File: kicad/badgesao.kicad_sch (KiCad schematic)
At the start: 62 parts, among them J1 DISP_DBG, J2 DEBUG, J3 USB_C_Receptacle_USB2.0_16P, Q1 NPN_BEC, SW1 UP, SW2 DOWN, SW3 LEFT, SW4 RIGHT, SW5 B, SW6 A, SW7 RESET, SW8 BOOTSEL, U1 3V3LDO, U2 32Mb QSPI, U3 LSM6DS3, U4 TPS61022, U6 RP2040, X1 Simple_Addon_v2, Y1 12M

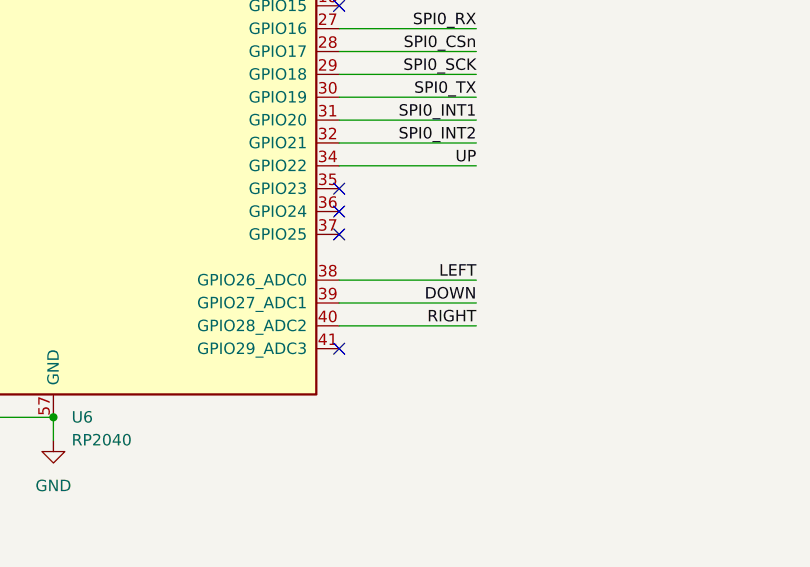
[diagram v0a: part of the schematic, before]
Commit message: connected buzzer and sel nets
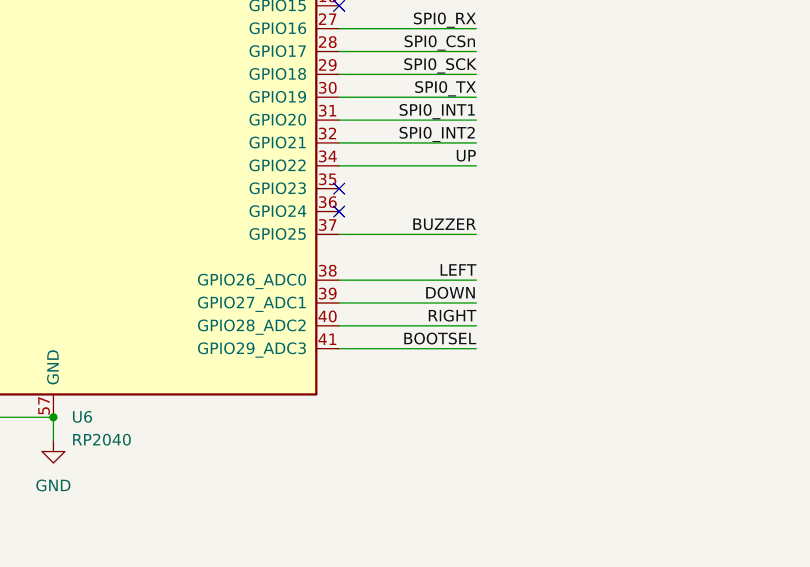
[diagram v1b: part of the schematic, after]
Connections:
- net BOOTSEL: now also U6.41 (GPIO29_ADC3)
- net BUZZER: now also U6.37 (GPIO25)
- no-connect marks 12 -> 10
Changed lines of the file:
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@@
-	)
-	(no_connect
-		(at 151.13 203.2)
 	)
 	(no_connect
@@
 	)
 	(no_connect
-		(at 151.13 215.9)
-	)
-	(no_connect
 		(at 359.41 182.88)
 	)
@@
 	(wire
 		(pts
+			(xy 151.13 215.9) (xy 166.37 215.9)
+		)
+		(stroke
+			(width 0)
+			(type default)
+		)
+	)
+	(wire
+		(pts
 			(xy 276.86 127) (xy 287.02 127)
 		)
@@
 		(pts
 			(xy 151.13 132.08) (xy 162.56 132.08)
+		)
+		(stroke
+			(width 0)
+			(type default)
+		)
+	)
+	(wire
+		(pts
+			(xy 166.37 203.2) (xy 151.13 203.2)
 		)
 		(stroke
@@
 		)
 	)
+	(label "BUZZER"
+		(at 166.37 203.2 180)
+		(fields_autoplaced yes)
+		(effects
+			(font
+				(size 1.27 1.27)
+			)
+			(justify right bottom)
+		)
+	)
 	(label "BLINKENLIGHT"
 		(at 166.37 154.94 180)
@@
 		)
 	)
+	(label "BOOTSEL"
+		(at 166.37 215.9 180)
+		(fields_autoplaced yes)
+		(effects
+			(font
+				(size 1.27 1.27)
+			)
+			(justify right bottom)
+		)
+	)

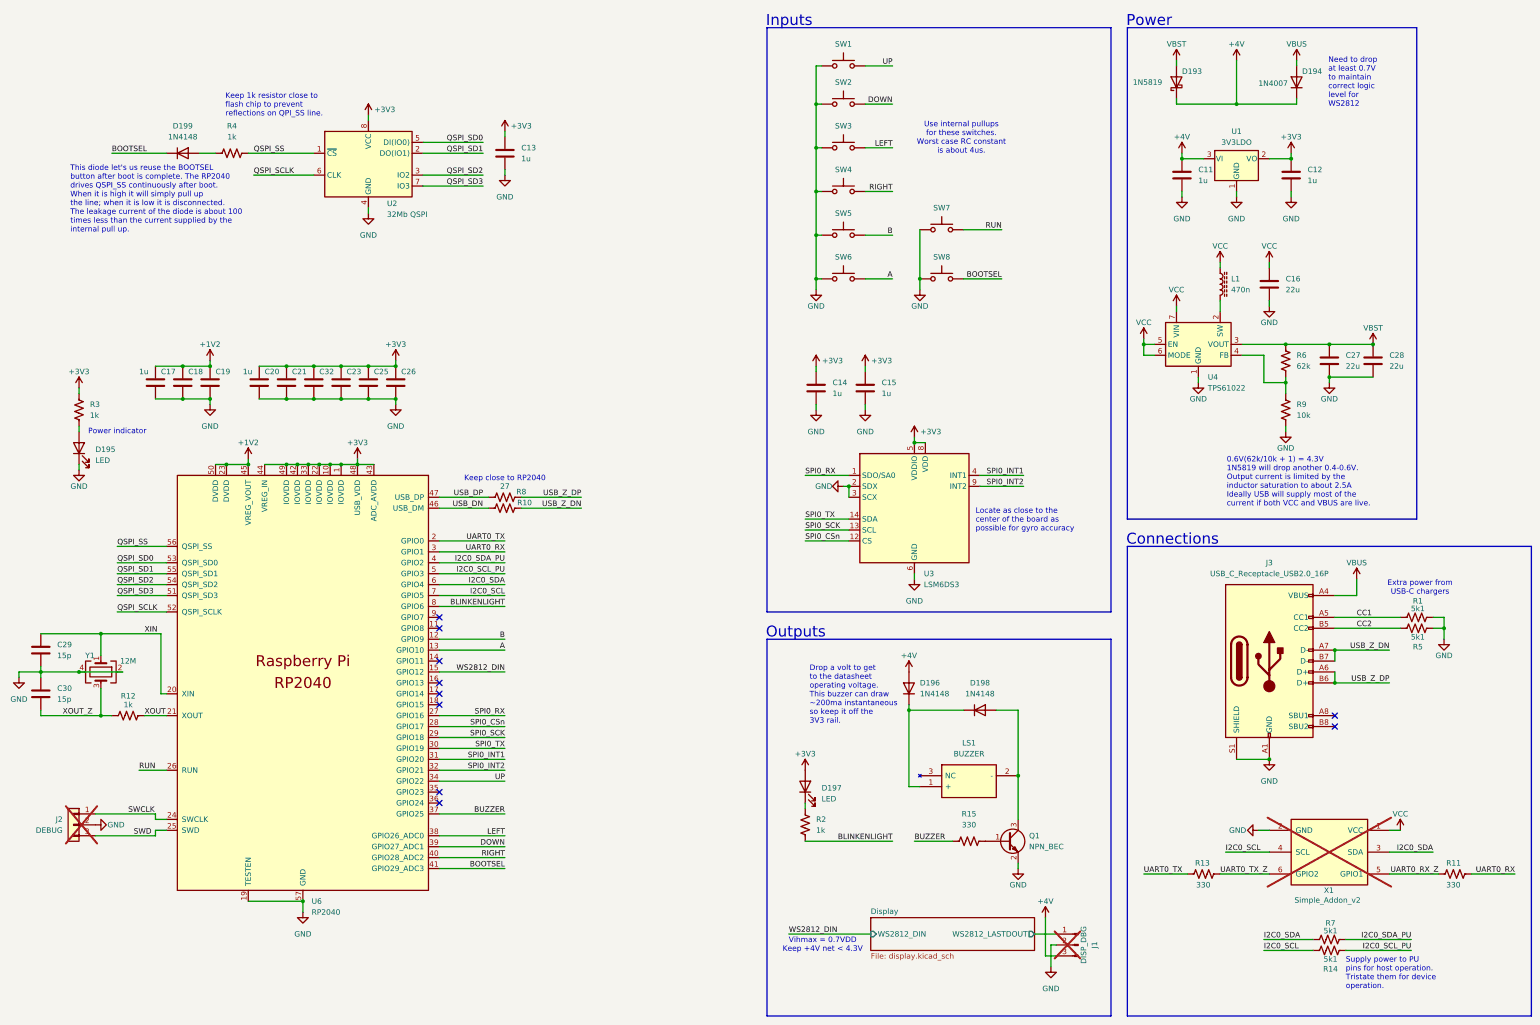
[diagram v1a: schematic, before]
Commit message: fixed all rev0 issues
connected buzzer and bootsel nets
changed IMU to I2C mode
changed IMU to the cheaper -C model
changed all buttons to PTS815
changed order of WS2812s so that the frame buffer can be shifted monolithically
changed boost converter feedback network to use JLCPCB basic parts
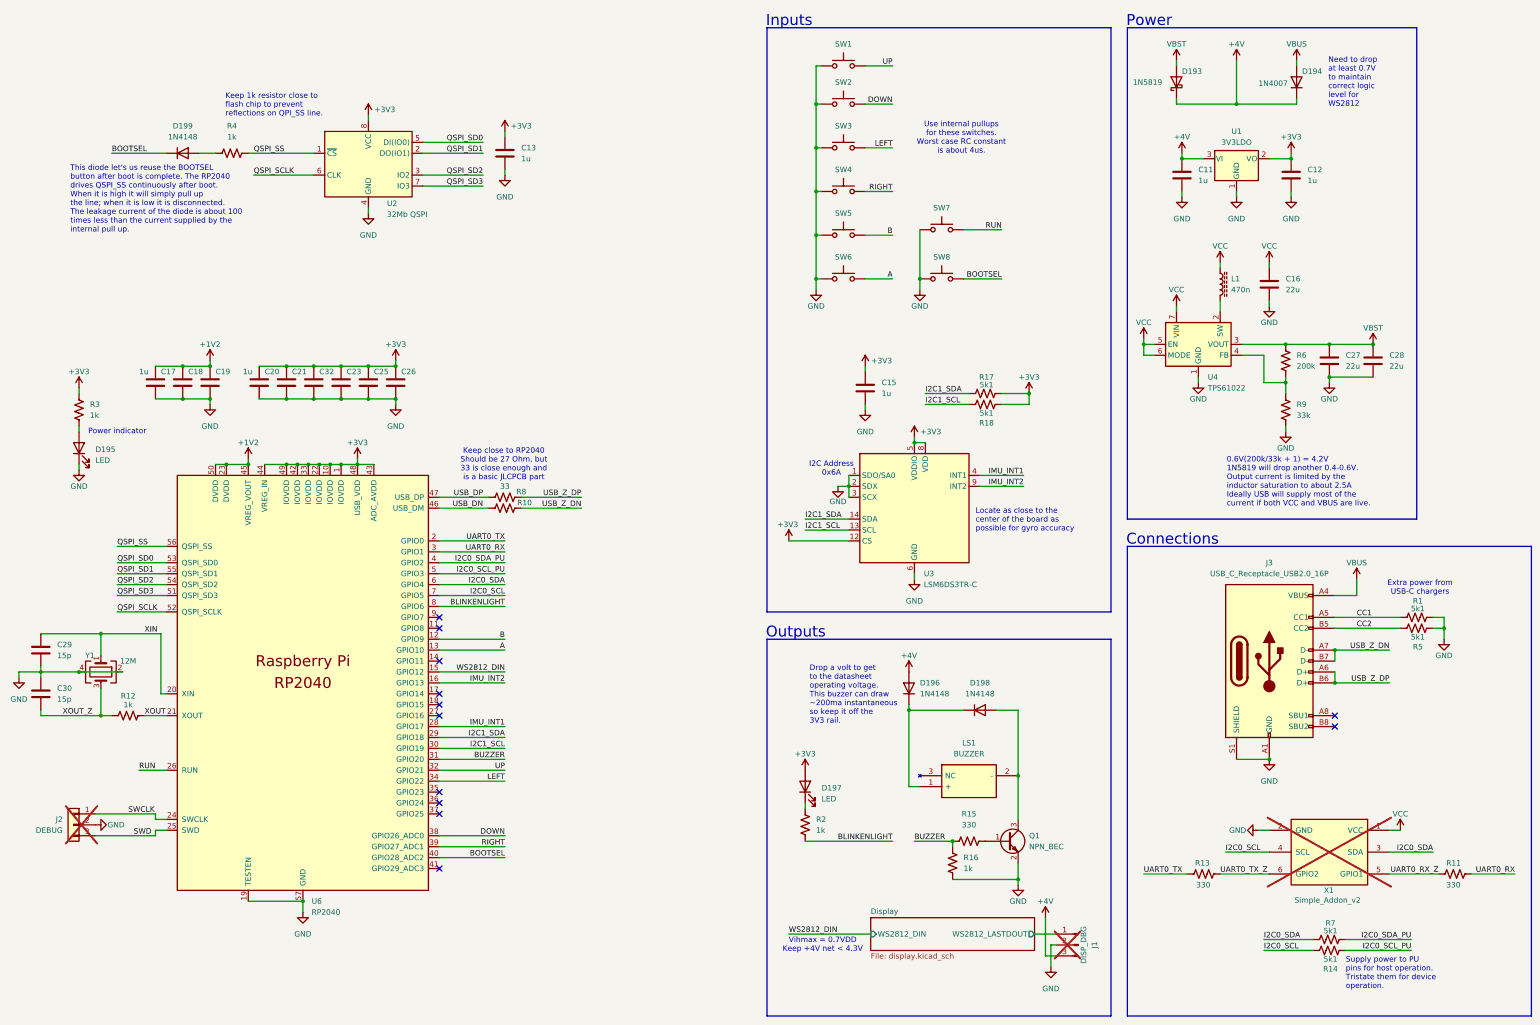
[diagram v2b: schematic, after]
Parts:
- removed C14: 1u, Capacitor_SMD:C_0402_1005Metric, symbol Device:C
- added R16: 1k, Resistor_SMD:R_0402_1005Metric, symbol Device:R_US
- added R17, R18: 5k1, Resistor_SMD:R_0402_1005Metric, symbol Device:R_US
- R10, R8: value 27 -> 33; Digikey_Part P27.0LCT-ND -> P33.0LCT-ND
- R6: value 62k -> 200k; Digikey_Part 311-62.0KLRCT-ND -> RMCF0402FT200KCT-ND; LCSC C2929930 -> C25764; Manufacturer_Name FOJAN -> UNI-ROYAL(Uniroyal Elec); Manufacturer_Part_Number FRC0402J623TS -> 0402WGF2003TCE
- R9: value 10k -> 33k; Digikey_Part 1276-3431-1-ND -> A129645CT-ND; LCSC C25744 -> C25779; Manufacturer_Part_Number 0402WGF1002TCE -> 0402WGF3302TCE
- SW1, SW2, SW3, SW4, SW5, SW6: Digikey_Part CKN10502CT-ND -> CKN12215-1-ND; LCSC C116501 -> C2689510; Manufacturer_Part_Number PTS810SJM250SMTRLFS -> PTS815SJM250SMTRLFS
- SW7, SW8: footprint kmj_custom:PTS830GM140SMTRLFS -> kmj_custom:SW_SPST_PTS810; Digikey_Part CKN10588CT-ND -> CKN12215-1-ND; LCSC C221902 -> C2689510; Manufacturer_Part_Number PTS830GG140SMTRLFS -> PTS815SJM250SMTRLFS
- U3: value LSM6DS3 -> LSM6DS3TR-C; Digikey_Part 497-15383-1-ND -> 497-LSM6DS3TR-CTR-ND; LCSC C95230 -> C967633; Manufacturer_Part_Number LSM6DS3TR -> LSM6DS3TR-C
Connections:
- net +3V3: now also U3.12 (CS), R17.1, R18.1
- net BOOTSEL: now also U6.40 (GPIO28_ADC2); no longer U6.41 (GPIO29_ADC3)
- net BUZZER: now also U6.31 (GPIO20), R16.2; no longer U6.37 (GPIO25)
- net DOWN: now also U6.38 (GPIO26_ADC0); no longer U6.39 (GPIO27_ADC1)
- net GND: now also U3.1 (SDO/SA0), R16.1
- net LEFT: now also U6.34 (GPIO22); no longer U6.38 (GPIO26_ADC0)
- net RIGHT: now also U6.39 (GPIO27_ADC1); no longer U6.40 (GPIO28_ADC2)
- net UP: now also U6.32 (GPIO21); no longer U6.34 (GPIO22)
- net IMU_INT2: now reaches U6.16 (GPIO13)
- net IMU_INT2: now also U3.9 (INT2)
- net SPI0_CSn renamed IMU_INT1
- net IMU_INT1: now also U3.4 (INT1); no longer U3.12 (CS)
- removed net SPI0_INT1: U3.4 (INT1), U6.31 (GPIO20)
- removed net SPI0_INT2: U3.9 (INT2), U6.32 (GPIO21)
- net SPI0_RX: no longer names the net of U6.27 (GPIO16)
- net SPI0_RX: no longer U3.1 (SDO/SA0)
- net SPI0_SCK renamed I2C1_SCL
- net I2C1_SCL: now also U6.30 (GPIO19), R18.2; no longer U6.29 (GPIO18)
- net SPI0_TX renamed I2C1_SDA
- net I2C1_SDA: now also U6.29 (GPIO18), R17.2; no longer U6.30 (GPIO19)
- no-connect marks 10 -> 12
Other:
- note added: "0.6V(200k/33k + 1) = 4.2V 1N5819 will drop another 0.4-0.6V. Output current is limited by the inductor saturation to about 2.5A Ideally USB will supply most of the current if both VCC and VBUS are live."
- note added: "I2C Address 0x6A"
- note added: "Keep close to RP2040 Should be 27 Ohm, but 33 is close enough and is a basic JLCPCB part"
- note removed: "0.6V(62k/10k + 1) = 4.3V 1N5819 will drop another 0.4-0.6V. Output current is limited by the inductor saturation to about 2.5A Ideally USB will supply most of the current if both VCC and VBUS are live."
- note removed: "Keep close to RP2040"
- title: (none) -> SuperXBit192
